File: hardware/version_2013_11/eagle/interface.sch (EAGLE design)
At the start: 19 parts

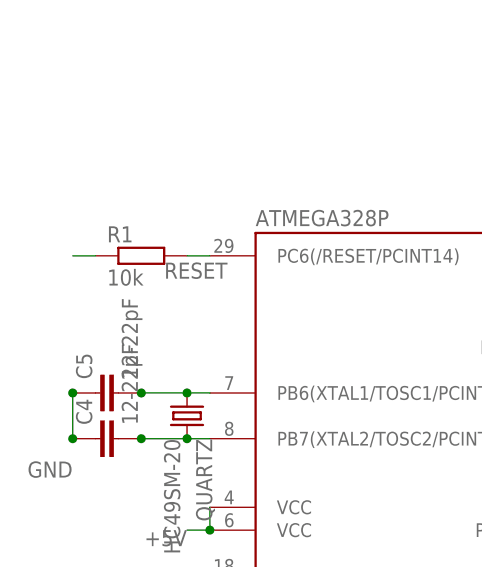
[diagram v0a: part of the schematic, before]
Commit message: version 2013_11 was in fact newer, now corrected
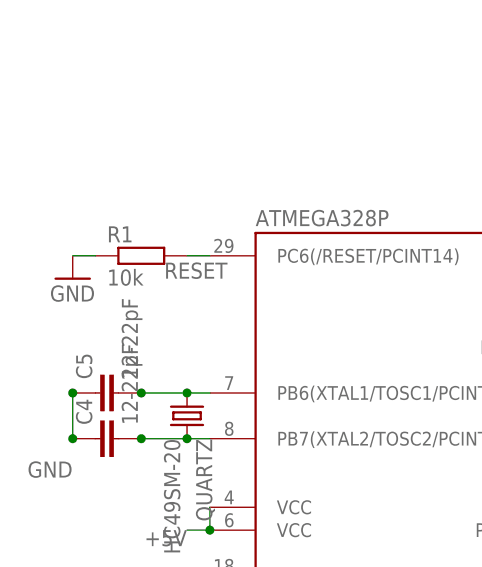
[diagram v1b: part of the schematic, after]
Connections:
- net +5V: no longer R1.1
- net GND: now also R1.1
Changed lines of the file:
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@@
 <grid distance="0.1" unitdist="inch" unit="inch" style="lines" multiple="1" display="no" altdistance="0.01" altunitdist="inch" altunit="inch"/>
 <layers>
-<layer number="1" name="Top" color="4" fill="1" visible="no" active="no"/>
-<layer number="2" name="Route2" color="1" fill="3" visible="no" active="no"/>
-<layer number="3" name="Route3" color="4" fill="3" visible="no" active="no"/>
-<layer number="4" name="Route4" color="1" fill="4" visible="no" active="no"/>
-<layer number="5" name="Route5" color="4" fill="4" visible="no" active="no"/>
-<layer number="6" name="Route6" color="1" fill="8" visible="no" active="no"/>
-<layer number="7" name="Route7" color="4" fill="8" visible="no" active="no"/>
-<layer number="8" name="Route8" color="1" fill="2" visible="no" active="no"/>
-<layer number="9" name="Route9" color="4" fill="2" visible="no" active="no"/>
-<layer number="10" name="Route10" color="1" fill="7" visible="no" active="no"/>
-<layer number="11" name="Route11" color="4" fill="7" visible="no" active="no"/>
-<layer number="12" name="Route12" color="1" fill="5" visible="no" active="no"/>
-<layer number="13" name="Route13" color="4" fill="5" visible="no" active="no"/>
-<layer number="14" name="Route14" color="1" fill="6" visible="no" active="no"/>
-<layer number="15" name="Route15" color="4" fill="6" visible="no" active="no"/>
-<layer number="16" name="Bottom" color="1" fill="1" visible="no" active="no"/>
-<layer number="17" name="Pads" color="2" fill="1" visible="no" active="no"/>
-<layer number="18" name="Vias" color="2" fill="1" visible="no" active="no"/>
-<layer number="19" name="Unrouted" color="6" fill="1" visible="no" active="no"/>
-<layer number="20" name="Dimension" color="15" fill="1" visible="no" active="no"/>
-<layer number="21" name="tPlace" color="7" fill="1" visible="no" active="no"/>
-<layer number="22" name="bPlace" color="7" fill="1" visible="no" active="no"/>
-<layer number="23" name="tOrigins" color="15" fill="1" visible="no" active="no"/>
-<layer number="24" name="bOrigins" color="15" fill="1" visible="no" active="no"/>
-<layer number="25" name="tNames" color="7" fill="1" visible="no" active="no"/>
-<layer number="26" name="bNames" color="7" fill="1" visible="no" active="no"/>
-<layer number="27" name="tValues" color="7" fill="1" visible="no" active="no"/>
-<layer number="28" name="bValues" color="7" fill="1" visible="no" active="no"/>
+<layer number="1" name="Top" color="4" fill="1" visible="yes" active="no"/>
+<layer number="2" name="Route2" color="1" fill="3" visible="yes" active="no"/>
+<layer number="3" name="Route3" color="4" fill="3" visible="yes" active="no"/>
+<layer number="4" name="Route4" color="1" fill="4" visible="yes" active="no"/>
+<layer number="5" name="Route5" color="4" fill="4" visible="yes" active="no"/>
+<layer number="6" name="Route6" color="1" fill="8" visible="yes" active="no"/>
+<layer number="7" name="Route7" color="4" fill="8" visible="yes" active="no"/>
+<layer number="8" name="Route8" color="1" fill="2" visible="yes" active="no"/>
+<layer number="9" name="Route9" color="4" fill="2" visible="yes" active="no"/>
+<layer number="10" name="Route10" color="1" fill="7" visible="yes" active="no"/>
+<layer number="11" name="Route11" color="4" fill="7" visible="yes" active="no"/>
+<layer number="12" name="Route12" color="1" fill="5" visible="yes" active="no"/>
+<layer number="13" name="Route13" color="4" fill="5" visible="yes" active="no"/>
+<layer number="14" name="Route14" color="1" fill="6" visible="yes" active="no"/>
+<layer number="15" name="Route15" color="4" fill="6" visible="yes" active="no"/>
+<layer number="16" name="Bottom" color="1" fill="1" visible="yes" active="no"/>
+<layer number="17" name="Pads" color="2" fill="1" visible="yes" active="no"/>
+<layer number="18" name="Vias" color="2" fill="1" visible="yes" active="no"/>
+<layer number="19" name="Unrouted" color="6" fill="1" visible="yes" active="no"/>
+<layer number="20" name="Dimension" color="15" fill="1" visible="yes" active="no"/>
+<layer number="21" name="tPlace" color="7" fill="1" visible="yes" active="no"/>
+<layer number="22" name="bPlace" color="7" fill="1" visible="yes" active="no"/>
+<layer number="23" name="tOrigins" color="15" fill="1" visible="yes" active="no"/>
+<layer number="24" name="bOrigins" color="15" fill="1" visible="yes" active="no"/>
+<layer number="25" name="tNames" color="7" fill="1" visible="yes" active="no"/>
+<layer number="26" name="bNames" color="7" fill="1" visible="yes" active="no"/>
+<layer number="27" name="tValues" color="7" fill="1" visible="yes" active="no"/>
+<layer number="28" name="bValues" color="7" fill="1" visible="yes" active="no"/>
 <layer number="29" name="tStop" color="7" fill="3" visible="no" active="no"/>
 <layer number="30" name="bStop" color="7" fill="6" visible="no" active="no"/>
@@
 <layer number="35" name="tGlue" color="7" fill="4" visible="no" active="no"/>
 <layer number="36" name="bGlue" color="7" fill="5" visible="no" active="no"/>
-<layer number="37" name="tTest" color="7" fill="1" visible="no" active="no"/>
-<layer number="38" name="bTest" color="7" fill="1" visible="no" active="no"/>
+<layer number="37" name="tTest" color="7" fill="1" visible="yes" active="no"/>
+<layer number="38" name="bTest" color="7" fill="1" visible="yes" active="no"/>
 <layer number="39" name="tKeepout" color="4" fill="11" visible="no" active="no"/>
 <layer number="40" name="bKeepout" color="1" fill="11" visible="no" active="no"/>
@@
 <layer number="44" name="Drills" color="7" fill="1" visible="no" active="no"/>
 <layer number="45" name="Holes" color="7" fill="1" visible="no" active="no"/>
-<layer number="46" name="Milling" color="3" fill="1" visible="no" active="no"/>
-<layer number="47" name="Measures" color="7" fill="1" visible="no" active="no"/>
-<layer number="48" name="Document" color="7" fill="1" visible="no" active="no"/>
-<layer number="49" name="Reference" color="7" fill="1" visible="no" active="no"/>
-<layer number="50" name="dxf" color="7" fill="1" visible="no" active="no"/>
-<layer number="51" name="tDocu" color="7" fill="1" visible="no" active="no"/>
-<layer number="52" name="bDocu" color="7" fill="1" visible="no" active="no"/>
-<layer number="53" name="tGND_GNDA" color="7" fill="9" visible="no" active="no"/>
-<layer number="54" name="bGND_GNDA" color="1" fill="9" visible="no" active="no"/>
-<layer number="56" name="wert" color="7" fill="1" visible="no" active="no"/>
-<layer number="57" name="tCAD" color="7" fill="1" visible="no" active="no"/>
+<layer number="46" name="Milling" color="3" fill="1" visible="yes" active="no"/>
+<layer number="47" name="Measures" color="7" fill="1" visible="yes" active="no"/>
+<layer number="48" name="Document" color="7" fill="1" visible="yes" active="no"/>
+<layer number="49" name="Reference" color="7" fill="1" visible="yes" active="no"/>
+<layer number="50" name="dxf" color="7" fill="1" visible="yes" active="no"/>
+<layer number="51" name="tDocu" color="7" fill="1" visible="yes" active="no"/>
+<layer number="52" name="bDocu" color="7" fill="1" visible="yes" active="no"/>
+<layer number="53" name="tGND_GNDA" color="7" fill="9" visible="yes" active="no"/>
+<layer number="54" name="bGND_GNDA" color="1" fill="9" visible="yes" active="no"/>
+<layer number="56" name="wert" color="7" fill="1" visible="yes" active="no"/>
+<layer number="57" name="tCAD" color="7" fill="1" visible="yes" active="no"/>
 <layer number="91" name="Nets" color="2" fill="1" visible="yes" active="yes"/>
 <layer number="92" name="Busses" color="1" fill="1" visible="yes" active="yes"/>
@@
 <part name="C3" library="rcl" deviceset="C-EU" device="C0805" value="100nF"/>
 <part name="R1" library="rcl" deviceset="R-EU_" device="R0805" value="10k"/>
+<part name="GND2" library="supply1" deviceset="GND" device=""/>
 <part name="I2C-RXTX" library="con-lstb" deviceset="MA03-2" device=""/>
 <part name="DIS1" library="display-hp" deviceset="HD-H101" device="" value=""/>
@@
 <instance part="C3" gate="G$1" x="111.76" y="104.14"/>
 <instance part="R1" gate="G$1" x="-5.08" y="68.58"/>
+<instance part="GND2" gate="1" x="-12.7" y="66.04"/>
 <instance part="I2C-RXTX" gate="1" x="198.12" y="12.7" rot="R180"/>
 <instance part="DIS1" gate="M" x="139.7" y="58.42"/>
@@
 </segment>
 <segment>
+<pinref part="R1" gate="G$1" pin="1"/>
+<pinref part="GND2" gate="1" pin="GND"/>
+<wire x1="-12.7" y1="68.58" x2="-10.16" y2="68.58" width="0.1524" layer="91"/>
+</segment>
+<segment>
 <pinref part="ATMEGA328P" gate="1" pin="GND@1"/>
 <pinref part="ATMEGA328P" gate="1" pin="GND@2"/>
@@
 <pinref part="C1" gate="G$1" pin="1"/>
 </segment>
-<segment>
-<pinref part="R1" gate="G$1" pin="1"/>
-<wire x1="-12.7" y1="68.58" x2="-10.16" y2="68.58" width="0.1524" layer="91"/>
-</segment>
 </net>
